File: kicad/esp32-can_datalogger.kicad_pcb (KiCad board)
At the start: 2 copper layers, 100 x 60 mm, 60 parts, among them J1 USB_C_Receptacle_USB2.0_16P, J2 USB_C_Receptacle_USB2.0_16P, J3 USB_C_Receptacle_USB2.0_16P, J4 USB_C_Receptacle_USB2.0_16P, J5 USB_C_Receptacle_USB2.0_16P, J6 USB_C_Receptacle_USB2.0_16P, J7 Conn_Coaxial, J8 MicroSD, J9 Conn_01x04_Socket, SW1 SW_Push, SW2 SW_Push, SW3 SW_Push, SW4 SW_Push, U2 PA1616D, U3 PI4ULS3V204LEX, U4 AZ1117-1.8, U5 TJA1051T, U6 TJA1051T, U7 ICM-20948

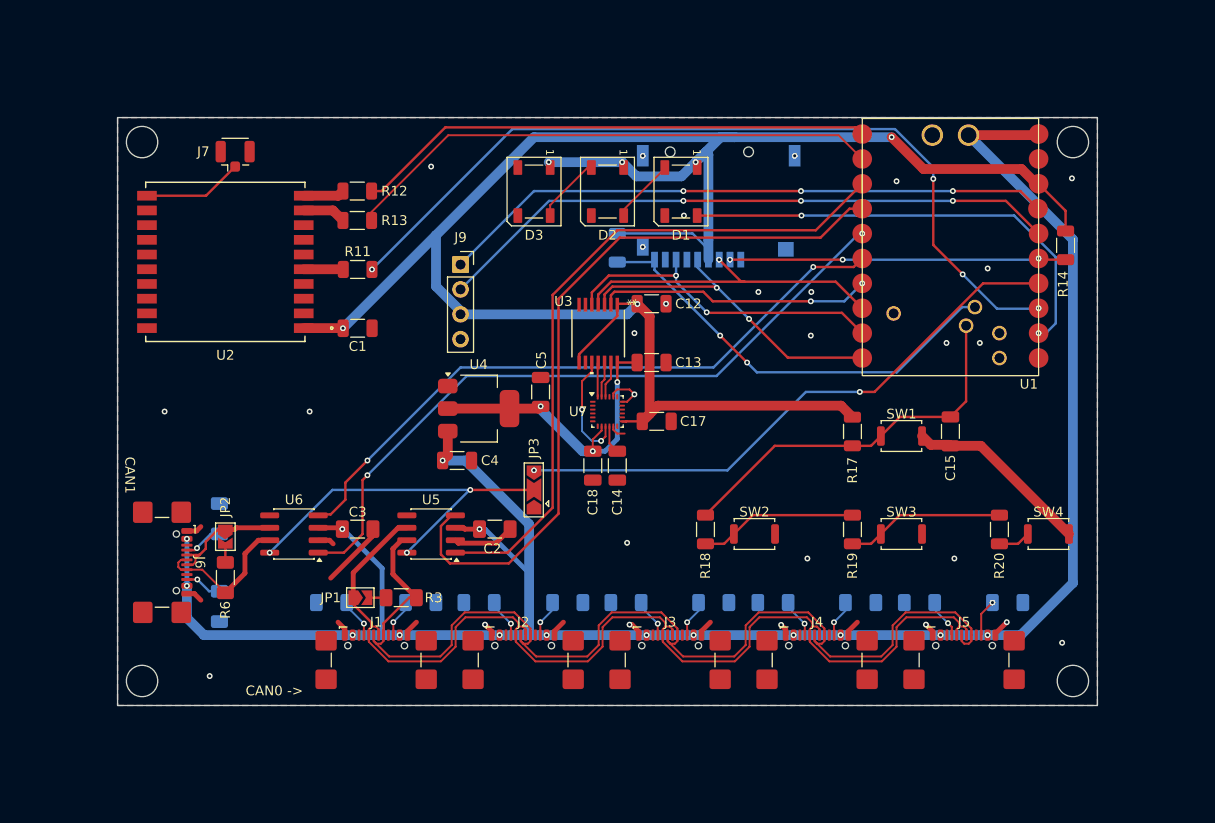
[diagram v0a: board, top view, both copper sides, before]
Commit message: make pcb smaller
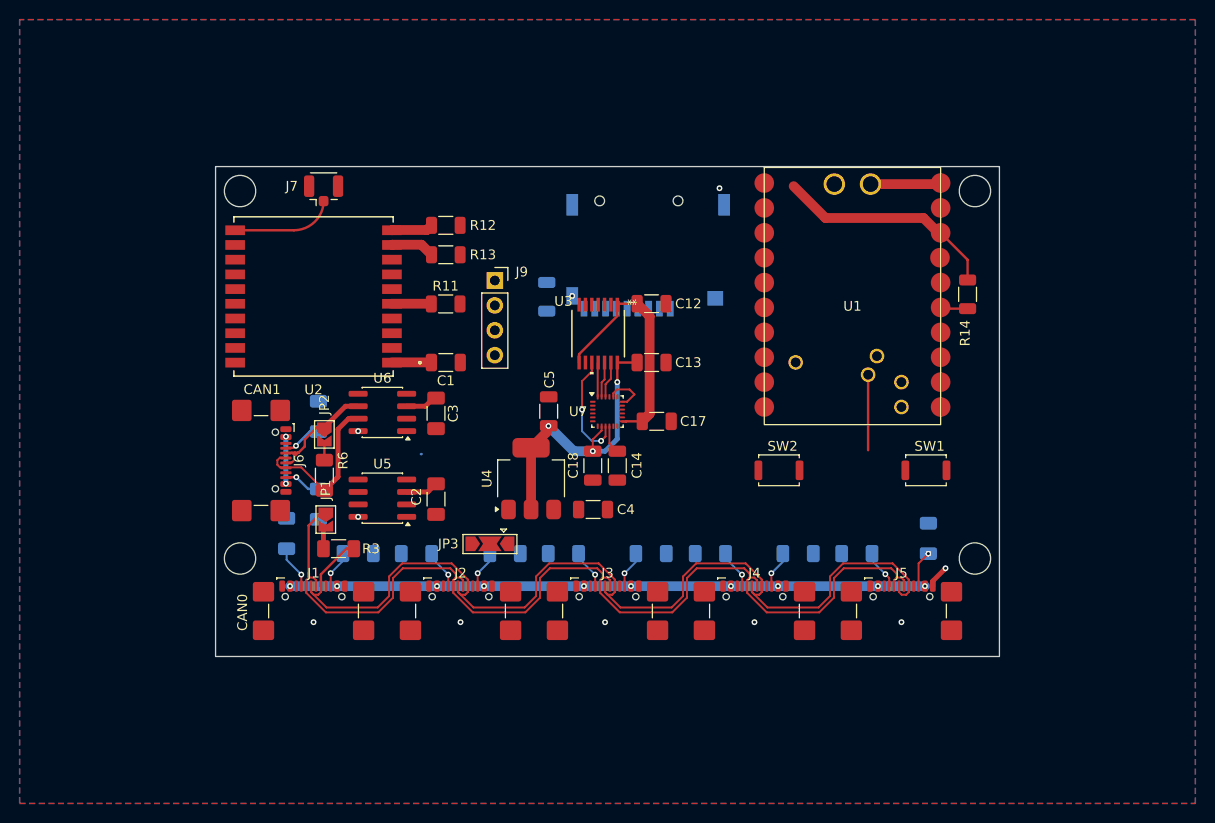
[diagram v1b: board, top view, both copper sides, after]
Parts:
- removed C15: 0.1uF, Capacitor_SMD:C_1206_3216Metric
- removed D1, D2, D3: WS2812B, LED_SMD:LED_WS2812B_PLCC4_5.0x5.0mm_P3.2mm
- removed R17: 47k, Resistor_SMD:R_1206_3216Metric
- removed R18: 16k, Resistor_SMD:R_1206_3216Metric
- removed R19: 30k, Resistor_SMD:R_1206_3216Metric
- removed R20: 91k, Resistor_SMD:R_1206_3216Metric
- removed SW3, SW4: SW_Push, Button_Switch_SMD:SW_Push_SPST_NO_Alps_SKRK
- moved U6 15.3 mm to (77.0, 100.1)
- moved C4 14.7 mm to (98.5, 110.0)
- moved JP2 14.5 mm to (71.1, 102.3)
- moved R6 14.5 mm to (71.1, 106.5)
- moved R10 14.5 mm to (70.5, 109.5)
- moved R9 14.5 mm to (70.5, 100.5)
- moved J6 14.5 mm to (63.5, 105.0)
- moved C3 14.3 mm to (82.5, 100.2), turned to 90 degrees
- moved R14 11.2 mm to (136.8, 88.0)
- moved U1 11.2 mm to (125.0, 86.8)
- moved R23 10.4 mm to (132.8, 113.0), turned to 90 degrees
- moved R12 9.69 mm to (83.5, 81.0)
- moved R13 9.69 mm to (83.5, 84.0)
- moved J7 9.69 mm to (71.0, 77.0)
- moved U2 9.67 mm to (70.0, 88.3)
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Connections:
- net BUTS renamed BUT1
- SW2 pad 1: Net-(R18-Pad2) -> BUT2
- U1 pad 12: ARGB_DIN -> BUT2
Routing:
- net +3.3V: track 210.2 -> 51.1 mm, vias 6 -> 0
- net +5V: track 209.1 -> 83.3 mm, vias 15 -> 12
- net GPS_FIX: track 86.2 -> 0.00 mm, vias 4 -> 0
- net /C0RX: track 75.7 -> 0.00 mm
- net /C1TX: track 72.2 -> 0.00 mm, vias 2 -> 0
- net /C0TX: track 69.8 -> 0.00 mm
- net /C1RX: track 67.3 -> 0.00 mm, vias 2 -> 0
- net I2C_SCK: track 64.1 -> 0.00 mm, vias 3 -> 0
- net I2C_SDA: track 62.8 -> 0.00 mm, vias 3 -> 0
- net Net-(JP3-B): track 59.4 -> 0.00 mm, vias 2 -> 0
- net GPS_TX: track 55.2 -> 0.00 mm
- net GPS_RX: track 53.0 -> 0.00 mm
- net GND: track 58.9 -> 6.80 mm, vias 27 -> 8
- net ARGB_DIN: track 47.3 -> 0.00 mm, vias 2 -> 0
- net SD_CD: track 44.7 -> 0.00 mm, vias 2 -> 0
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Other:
- board size 100 x 60 mm -> 80 x 50 mm
- board text added: "CAN0"
- board text removed: "CAN0 ->"

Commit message: make smaller still
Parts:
- removed J4, J5: USB_C_Receptacle_USB2.0_16P, Connector_USB:USB_C_Receptacle_GCT_USB4110
- removed JP2: SolderJumper_2_Open, Jumper:SolderJumper-2_P1.3mm_Open_TrianglePad1.0x1.5mm
- removed JP3: SolderJumper_3_Open, Jumper:SolderJumper-3_P2.0mm_Open_TrianglePad1.0x1.5mm
- removed R16, R21, R22, R23: 5K1, Resistor_SMD:R_1206_3216Metric_Pad1.30x1.75mm_HandSolder
- removed R6: 120, Resistor_SMD:R_1206_3216Metric_Pad1.30x1.75mm_HandSolder
- J7: footprint Connector_Coaxial:U.FL_Hirose_U.FL-R-SMT-1_Vertical -> Connector_Coaxial:SMA_BAT_Wireless_BWSMA-KWE-Z001
- R1, R10, R2, R3, R4, R5, R7, R8, R9: footprint Resistor_SMD:R_1206_3216Metric_Pad1.30x1.75mm_HandSolder -> Resistor_SMD:R_0402_1005Metric_Pad0.72x0.64mm_HandSolder
- R11, R12, R13, R14, R15: footprint Resistor_SMD:R_1206_3216Metric -> Resistor_SMD:R_0402_1005Metric_Pad0.72x0.64mm_HandSolder
- moved J9 44.7 mm to (133.0, 82.2)
- moved R14 31.5 mm to (105.2, 87.2)
- moved SW1 23.4 mm to (110.0, 112.5)
- moved C1 21.7 mm to (97.0, 78.0), turned to 90 degrees
- moved U2 17.4 mm to (87.0, 84.8), turned to -90 degrees
- moved R11 15.3 mm to (96.9, 81.8)
- moved J1 15.0 mm to (85.0, 121.5)
- moved J2 15.0 mm to (100.0, 121.5)
- moved J3 15.0 mm to (115.0, 121.5)
- moved R1 15.0 mm to (89.5, 114.5)
- moved R4 15.0 mm to (95.5, 114.5)
- moved R5 15.0 mm to (104.5, 114.5)
- moved R7 15.0 mm to (110.5, 114.5)
- moved R8 15.0 mm to (119.5, 114.5)
- moved R12 14.1 mm to (96.9, 85.2)
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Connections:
- U1 pad 14: Net-(JP3-B) -> /C0SX
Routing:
- net +5V: track 83.3 -> 4.80 mm, vias 12 -> 8
- net /CAN0L: track 101.9 -> 49.0 mm
- net /CAN0H: track 102.0 -> 49.4 mm
- net +3.3V: track 51.1 -> 10.7 mm
- net /CAN1H: track 16.7 -> 2.44 mm
- net /CAN1L: track 12.4 -> 3.92 mm
- net BUT1: track 7.71 -> 0.00 mm
- net Net-(J7-In): track 6.00 -> 0.00 mm
- net Net-(U2-TX0): track 4.47 -> 0.00 mm
- net Net-(J1-CC1): track 4.44 -> 0.00 mm, vias 1 -> 0
- net Net-(U2-RX0): track 4.24 -> 0.00 mm
- net Net-(J6-CC1): track 4.03 -> 0.00 mm, vias 1 -> 0
- net Net-(U2-3D-FIX): track 4.02 -> 0.00 mm
- net Net-(J6-CC2): track 3.82 -> 0.00 mm, vias 1 -> 0
- net Net-(J5-CC2): track 3.73 -> 0.00 mm, vias 1 -> 0
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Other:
- board size 80 x 50 mm -> 60 x 50 mm

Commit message: layout refinement
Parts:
- added C15: 0.1uF, Capacitor_SMD:C_0402_1005Metric_Pad0.74x0.62mm_HandSolder, B.Cu at (104.2, 92.4)
- C1, C12, C13, C14, C17, C18: footprint Capacitor_SMD:C_1206_3216Metric -> Capacitor_SMD:C_0402_1005Metric_Pad0.74x0.62mm_HandSolder
- C4, C5: footprint Capacitor_SMD:C_1206_3216Metric -> Capacitor_SMD:C_1206_3216Metric_Pad1.33x1.80mm_HandSolder
- R14: moved to B.Cu
- moved J9 50.3 mm to (92.4, 112.0), turned to 90 degrees
- moved C4 10.5 mm to (92.1, 105.9), turned to -90 degrees
- moved U4 7.89 mm to (93.2, 99.3), turned to 0 degrees
- moved R15 6.40 mm to (98.8, 92.3), turned to -90 degrees
- moved R3 5.96 mm to (83.0, 114.4), turned to -90 degrees
- moved R8 5.53 mm to (120.0, 120.0)
- moved R2 5.52 mm to (80.0, 120.0)
- moved R4 5.52 mm to (95.0, 120.0)
- moved R7 5.52 mm to (110.0, 120.0)
- moved R1 5.52 mm to (90.0, 120.0)
- moved R5 5.52 mm to (105.0, 120.0)
- moved R14 5.40 mm to (106.5, 92.4), turned to -90 degrees
- moved R10 5.00 mm to (75.5, 109.5)
- moved R9 5.00 mm to (75.5, 100.5)
- moved C5 4.87 mm to (96.4, 104.2), turned to 180 degrees
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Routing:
- net +1V8: track 31.6 -> 1.39 mm, vias 3 -> 0
- net /CAN0L: track 49.0 -> 62.3 mm
- net /CAN0H: track 49.4 -> 62.2 mm
- net /MISO_1V8: track 11.5 -> 0.00 mm, vias 2 -> 0
- net +3.3V: track 10.7 -> 4.25 mm
- net +5V: track 4.80 -> 0.00 mm, vias 8 -> 0
- net GND: track 4.45 -> 0.00 mm
- net /CS_IMU_1V8: track 3.73 -> 0.00 mm
- net unconnected-(U2-NC-Pad20): track 3.69 -> 0.00 mm
- net Net-(U7-REGOUT): track 3.67 -> 0.00 mm
- net /SCK_1V8: track 3.62 -> 0.00 mm
- net /MOSI_1V8: track 3.45 -> 0.00 mm
- net CS_SD: track 0.00 -> 2.25 mm
- net SD_CD: track 0.00 -> 2.17 mm
- net Net-(JP1-B): track 0.00 -> 1.88 mm
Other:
- board size 60 x 50 mm -> 55 x 50 mm

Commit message: update layout and schematic
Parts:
- added R16: 10K, Resistor_SMD:R_0402_1005Metric_Pad0.72x0.64mm_HandSolder, F.Cu at (111.5, 112.4)
- added R17: 10K, Resistor_SMD:R_0402_1005Metric_Pad0.72x0.64mm_HandSolder, F.Cu at (118.5, 112.4)
- moved SW1 15.0 mm to (122.5, 112.5), turned to 180 degrees
- moved SW2 15.0 mm to (107.5, 112.5), turned to 180 degrees
- moved C13 3.46 mm to (103.5, 97.4), turned to -90 degrees
- moved R10 2.07 mm to (77.5, 110.0)
- moved R9 2.06 mm to (77.5, 100.0)
- moved C4 1.49 mm to (92.5, 104.5), turned to 0 degrees
- moved C5 1.27 mm to (97.5, 104.9), turned to -90 degrees
- moved C2 1.25 mm to (86.4, 113.0)
- moved C3 1.25 mm to (86.4, 104.3)
- moved J9 1.14 mm to (91.4, 112.5)
- moved C18 0.54 mm to (100.2, 103.8), turned to 180 degrees
- moved J6 0.15 mm to (76.0, 105.0)
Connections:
- SW1 pad 1: BUT1 -> BUTS
- SW1 pad 2: GND -> Net-(R17-Pad2)
- SW2 pad 1: BUT2 -> BUTS
- U1 pad 10: SCK -> BUTS
- U1 pad 12: BUT2 -> unconnected-(U1-GPIO9_(BOOT)-Pad12)
- U1 pad 14: /C0SX -> CS_SD
- U1 pad 15: CS_SD -> CS_IMU
- U1 pad 3: /C0TX -> MOSI
- U1 pad 4: /C0RX -> MISO
- U1 pad 5: /C1TX -> SCK
- U1 pad 7: CS_IMU -> /C1TX
- U1 pad 8: MOSI -> /C0RX
- U1 pad 9: MISO -> /C0TX
- U5 pad 8: /C0SX -> GND
- U6 pad 8: /C0SX -> GND
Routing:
- net +5V: track 0.00 -> 116.5 mm, vias 0 -> 12
- net GPS_FIX: track 0.00 -> 47.8 mm, vias 0 -> 2
- net CS_IMU: track 0.00 -> 27.4 mm, vias 0 -> 2
- net /C0RX: track 0.00 -> 25.3 mm
- net BUTS: track 0.00 -> 23.8 mm
- net /C0TX: track 0.00 -> 23.3 mm
- net CS_SD: track 2.25 -> 23.7 mm, vias 0 -> 1
- net Net-(U2-RX0): track 0.00 -> 20.3 mm
- net +1V8: track 1.39 -> 19.5 mm
- net Net-(U2-TX0): track 0.00 -> 17.1 mm
- net /MISO_1V8: track 0.00 -> 12.5 mm, vias 0 -> 2
- net Net-(U2-3D-FIX): track 0.00 -> 11.3 mm
- net MOSI: track 0.00 -> 11.0 mm, vias 0 -> 1
- net MISO: track 0.00 -> 10.7 mm, vias 0 -> 1
- net SCK: track 0.00 -> 9.27 mm, vias 0 -> 2
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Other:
- outline, holes or cut-outs redrawn

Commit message: complete layout - TODO check changes work
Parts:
- J1, J2, J3, J6: footprint Connector_USB:USB_C_Receptacle_GCT_USB4110 -> esp32-can_datalogger:USB_C_Receptacle_GCT_USB4110-grounded shield
- moved R14 18.4 mm to (92.0, 81.1), turned to 90 degrees
- moved J8 15.5 mm to (93.2, 91.7), turned to 180 degrees
- moved C15 15.1 mm to (94.2, 81.1), turned to -90 degrees
- moved R15 11.2 mm to (99.8, 81.2), turned to 90 degrees
- moved C5 0.50 mm to (97.5, 105.4)
- moved R3 0.30 mm to (83.0, 114.7)
- moved J7 0.25 mm to (76.7, 85.0)
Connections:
- U1 pad 26: BUT1 -> unconnected-(U1-GPIO22-Pad26)
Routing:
- net GND: track 5.93 -> 139.2 mm, vias 4 -> 32
- net +3.3V: track 6.53 -> 130.5 mm, vias 0 -> 8
- net I2C_SDA: track 0.00 -> 43.2 mm, vias 0 -> 1
- net I2C_SCK: track 0.00 -> 39.6 mm, vias 0 -> 1
- net SD_CD: track 2.10 -> 29.4 mm, vias 0 -> 1
- net /C1TX: track 0.00 -> 23.0 mm, vias 0 -> 2
- net /C1RX: track 0.00 -> 21.2 mm, vias 0 -> 2
- net CS_SD: track 23.7 -> 44.0 mm
- net +5V: track 116.5 -> 134.9 mm, vias 12 -> 11
- net SCK: track 9.27 -> 24.3 mm
- net +1V8: track 19.5 -> 29.0 mm, vias 0 -> 2
- net MOSI: track 11.0 -> 18.8 mm
- net MISO: track 10.7 -> 17.2 mm
- net Net-(J6-CC1): track 0.00 -> 4.89 mm, vias 0 -> 1
- net Net-(J3-CC1): track 0.00 -> 4.45 mm, vias 0 -> 1
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
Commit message: add vbackup 1220 cell
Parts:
- added BT1: Battery_Cell, esp32-can_datalogger:BAT_1056, B.Cu at (116.5, 85.6)
- added C6: 1uF, Capacitor_SMD:C_0402_1005Metric_Pad0.74x0.62mm_HandSolder, B.Cu at (92.5, 76.7)
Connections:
- U1 pad 10: BUTS -> /C0TX
- U1 pad 14: CS_SD -> unconnected-(U1-GPIO15-Pad14)
- U1 pad 26: unconnected-(U1-GPIO22-Pad26) -> ACC_INT
- U1 pad 27: unconnected-(U1-GPIO23-Pad27) -> CS_SD
- U1 pad 8: /C0RX -> BUTS
- U1 pad 9: /C0TX -> /C0RX
- U2 pad 4: unconnected-(U2-VBACKUP-Pad4) -> VBACKUP
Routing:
- net VBACKUP: track 0.00 -> 25.6 mm, vias 0 -> 1
- net ACC_INT: track 0.00 -> 25.4 mm, vias 0 -> 3
- net CS_SD: track 44.0 -> 32.4 mm, vias 1 -> 0
- net BUTS: track 23.9 -> 29.6 mm
- net /C0RX: track 25.3 -> 23.1 mm
- net /C0TX: track 23.3 -> 21.9 mm
- net CS_IMU: track 26.7 -> 27.7 mm
- net I2C_SDA: track 43.2 -> 42.5 mm
- net +3.3V: track 130.5 -> 131.1 mm
- net GND: track 139.2 -> 138.9 mm, vias 32 -> 33
